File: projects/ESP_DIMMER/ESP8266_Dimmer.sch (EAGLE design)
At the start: 39 parts, among them IC1 LD117AS33TR, IC2 TINY24/44/84-SSU, Q1 IRF840

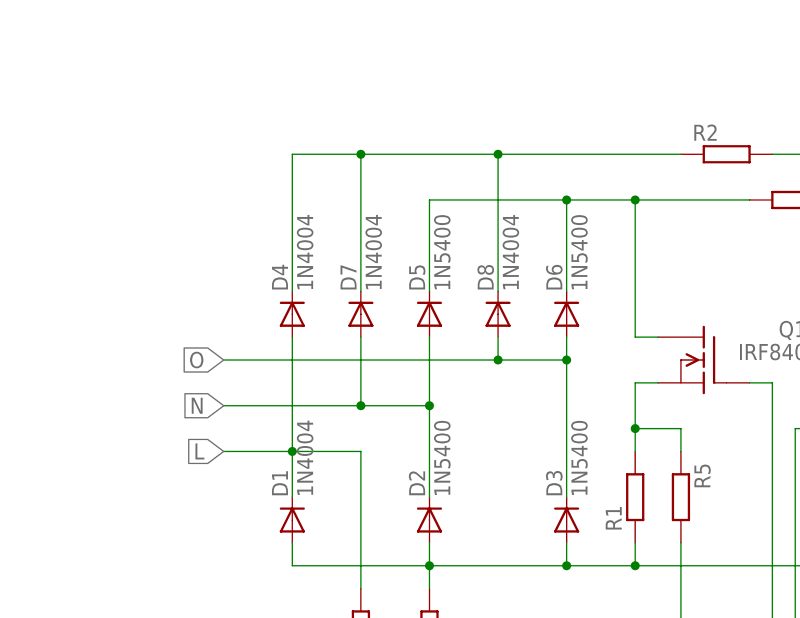
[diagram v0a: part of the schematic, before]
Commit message: Change wrong Diode after first Review
Signed-off-by: Juergen G. Schimmer <schimmi2@gmail.com>
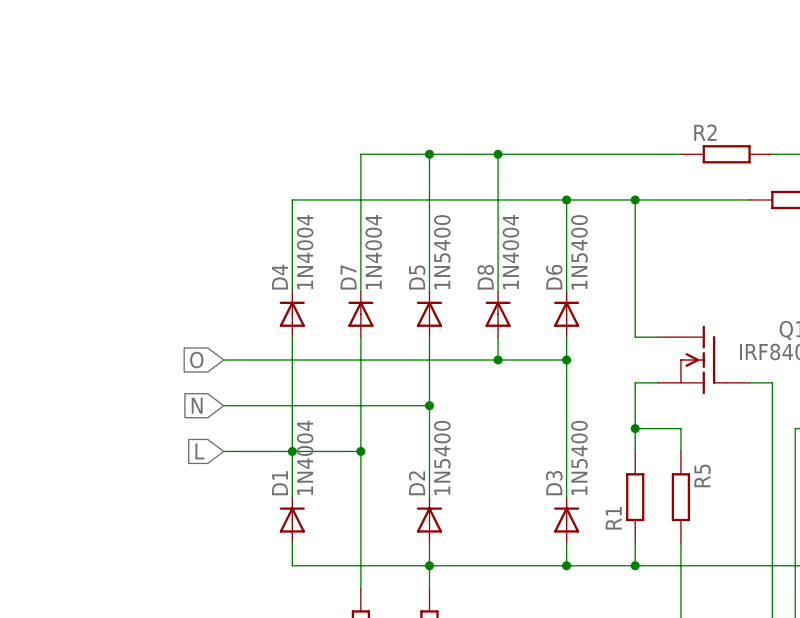
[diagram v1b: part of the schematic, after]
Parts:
- removed U$3: PCB68, hohlraumdose:PCB68
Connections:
- net L: now also D7.A
- net N: no longer D7.A
- net N$2: now also D4.C; no longer D5.C
- net N$3: now also D5.C; no longer D4.C
